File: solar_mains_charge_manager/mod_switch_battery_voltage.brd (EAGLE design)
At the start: 100 x 80 mm, 22 parts, among them IC1 ACS750LCA-050, X10 22-23-2041, X3 22-23-2031, X5 22-23-2031, X6 22-23-2041, X7 53047-15, X8 53047-15

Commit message: A lot of stuff
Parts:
- removed D1, D2, D3, D4, D8: 1N4004, diode:DO41-10
- removed D5, D7: (no value), diode:DO34Z7
- removed IC1: ACS750LCA-050, allegro:ACS75050
- removed OK2: PC817, optocoupler:DIL04
- removed R10, R12, R5, R9: (no value), resistor:0204/5
- removed R6, R7: (no value), resistor:0204/7
- removed U$1: NANO, Arduino-clone:NANO
- removed X10, X6: 22-23-2041, con-molex:22-23-2041
- removed X3, X5: 22-23-2031, con-molex:22-23-2031
- removed X7, X8: 53047-15, con-molex:53047-15
- added D6: (no value), diode:DO34Z7
- added OK1: PC817, optocoupler:DIL04
- added R1, R11, R2, R3, R4: (no value), resistor:0204/5
- added T1: TIP122, transistor:TO220
- added X1: 22-23-2051, con-molex:22-23-2051
- added X2: 22-23-2021, con-molex:22-23-2021
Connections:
- removed net N$1: U$1.3.3V, U$1.AREF, X7.13, X7.14
- removed net N$11: D1.C, D2.C, R7.2
- removed net N$12: OK2.4, U$1.D12, X8.1
- removed net N$13: D1.A, D3.C
- removed net N$15: D2.A, D4.C, R6.1
- removed net N$16: R6.2
- removed net N$17: U$1.D11, X3.2, X8.2
- removed net N$18: U$1.D10, X3.3, X8.3
- removed net N$19: U$1.D9, X6.3, X8.4
- removed net N$2: U$1.D13, X7.15
- removed net N$20: U$1.D8, X6.4, X8.5
- removed net N$21: U$1.RST, X6.2, X7.3
- removed net N$22: U$1.D7, X8.6
- removed net N$23: U$1.D6, X8.7
- removed net N$24: U$1.D5, X8.8
- removed net N$25: U$1.D4, X8.9
- removed net N$26: U$1.D3, X8.10
- removed net N$27: U$1.D2, X8.11
- removed net N$28: U$1.GND1, X8.12
- removed net N$29: U$1.RST1, X8.13
- removed net N$3: R10.2, R12.1, R9.2
- removed net N$30: U$1.RX1, X8.14
- removed net N$31: U$1.TX0, X8.15
- removed net N$32: U$1.5V, X7.4
- removed net N$33: U$1.A7, X7.5
- removed net N$34: U$1.A6, X7.6
- removed net N$35: U$1.A5, X7.7
- removed net N$36: U$1.A4, X7.8
- removed net N$37: U$1.A3, X7.9
- removed net N$38: U$1.A2, X7.10
- removed net N$39: D7.C, D8.C, R12.2, U$1.A1, X7.11
- removed net N$41: R10.1, X10.4
- removed net N$42: R9.1, X10.3
- removed net N$8: D3.A, D4.A, D5.A, OK2.2, R5.1
- removed net N$9: D5.C, OK2.1, R5.2, R7.1
- removed net VCC: IC1.1
- new net N$4: OK1.1, R3.1
- new net N$43: R1.2, R11.1, R2.2
- new net N$5: T1.2, X2.2
- new net N$6: R3.2, X1.2
- new net N$7: OK1.3, R4.2, T1.1
- net 12V: now also OK1.4, X1.4, X2.1; no longer U$1.RAW, X5.3, X7.1
- net BAT: now also R1.1, X1.3; no longer X10.2, X5.2
- net GND: now also D6.A, OK1.2, R2.1, R4.1, T1.3, X1.5; no longer D7.A, D8.A, IC1.2, OK2.3, U$1.GND, X10.1, X3.1, X5.1, X6.1, X7.2
- net N$40: now also D6.C, R11.2, X1.1; no longer U$1.A0, X7.12
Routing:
- net 12V: track 0.00 -> 32.4 mm
- net N$40: track 0.00 -> 18.1 mm
- net N$4: track 0.00 -> 13.2 mm
- net N$7: track 0.00 -> 8.67 mm
- net BAT: track 0.00 -> 8.67 mm
- net N$5: track 0.00 -> 6.88 mm
- net N$43: track 0.00 -> 5.08 mm
- net N$6: track 0.00 -> 5.08 mm
- added copper zone on layer 16, net GND
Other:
- board size 100 x 80 mm -> 42.9 x 19 mm

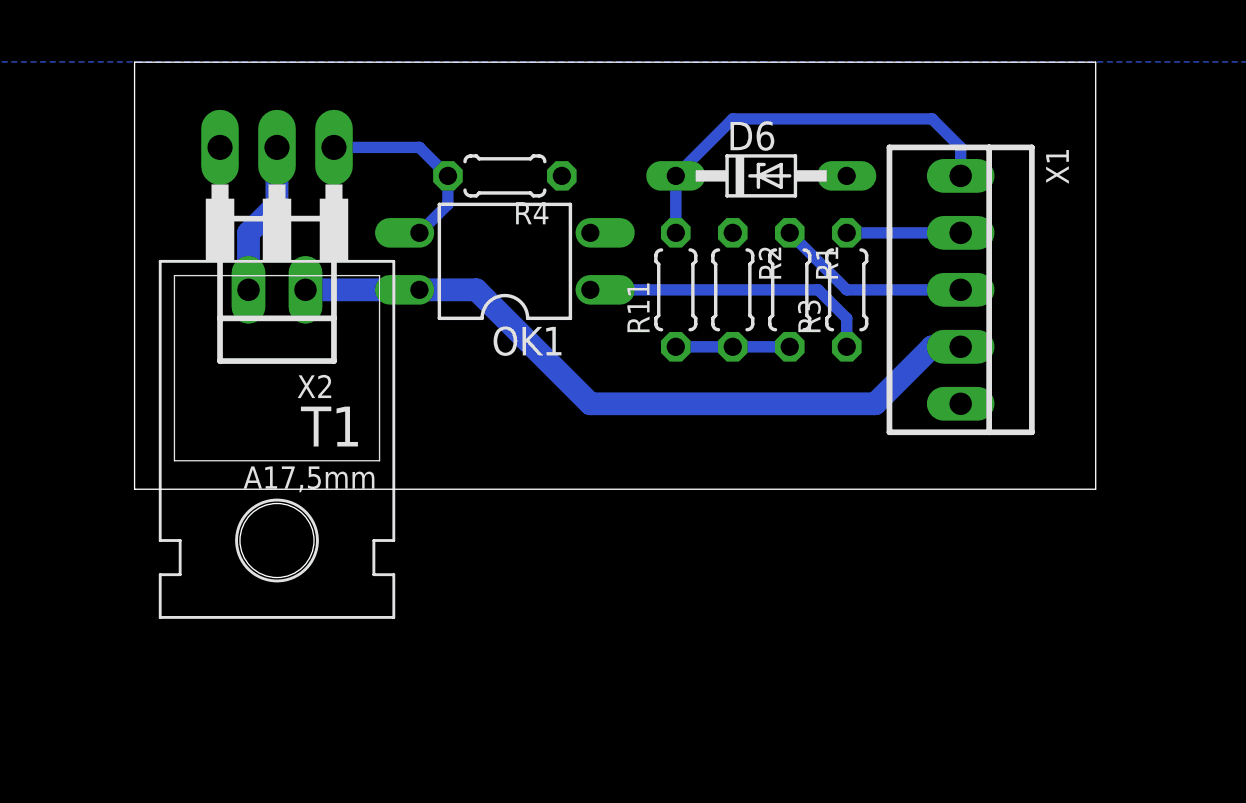
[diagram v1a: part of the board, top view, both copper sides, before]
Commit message: Finished board layout of mod_switch_battery_voltage and more work on psu_considerations.ods
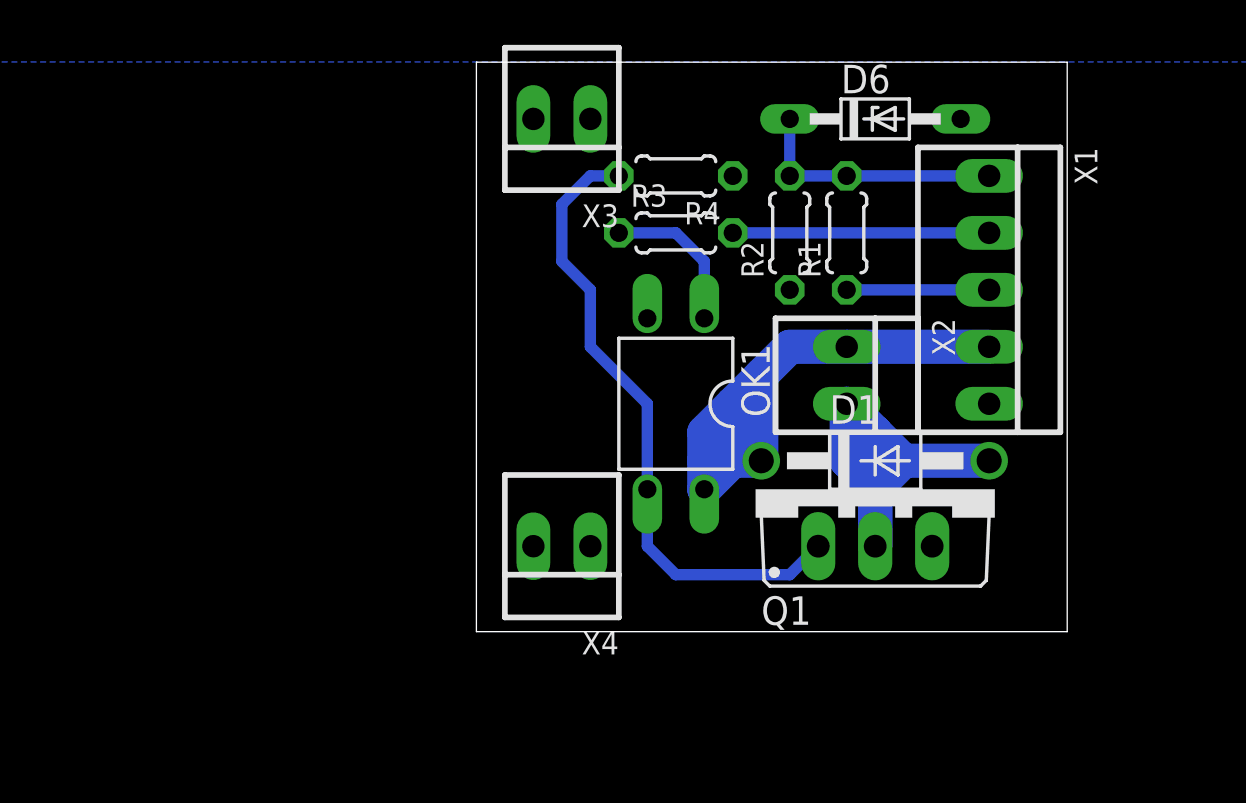
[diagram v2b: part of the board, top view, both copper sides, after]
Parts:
- removed R11: (no value), resistor:0204/5
- removed T1: TIP122, transistor:TO220
- added D1: 1N4004, diode:DO41-10
- added Q1: IRF540, transistor-power:TO220BV
- added X3, X4: 22-23-2021, con-molex:22-23-2021
- moved X2 25.7 mm to (38.1, 66.0), turned to 270 degrees
- moved OK1 9.92 mm to (30.5, 64.8), turned to 180 degrees
- moved R3 8.03 mm to (30.5, 72.4), turned to 0 degrees
- moved R4 7.62 mm to (30.5, 74.9)
- moved D6 5.68 mm to (39.4, 77.5)
- moved R1 3.59 mm to (38.1, 72.4), turned to 90 degrees
- moved R2 3.59 mm to (35.6, 72.4), turned to 90 degrees
- moved X1 1.27 mm to (44.5, 69.8)
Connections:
- removed net N$40: D6.C, R11.2, X1.1
- net 12V: now also D1.C
- net GND: now also Q1.S, X3.1, X3.2, X4.1, X4.2; no longer T1.3
- net N$43: now also D6.C, X1.1; no longer R11.1
- net N$5: now also D1.A, Q1.D; no longer T1.2
- net N$7: now also Q1.G; no longer T1.1
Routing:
- net N$7: track 8.67 -> 28.6 mm
- net N$40: track 18.1 -> 0.00 mm
- net N$5: track 6.88 -> 21.2 mm
- net N$6: track 5.08 -> 11.4 mm
- net N$43: track 5.08 -> 11.4 mm
- net N$4: track 13.2 -> 6.88 mm
- net 12V: track 32.4 -> 28.0 mm
- net BAT: track 8.67 -> 6.35 mm
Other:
- board size 42.9 x 19 mm -> 26.3 x 25.4 mm
